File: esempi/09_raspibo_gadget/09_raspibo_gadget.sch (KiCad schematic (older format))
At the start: 20 parts, among them IC1 ATTINY85-S, P1 USB_OTG, P2 CONN_01X01, P3 CONN_01X01, P4 CONN_01X01, P5 CONN_01X01, P6 CONN_01X01, P7 CONN_01X01, P8 CONN_01X01, P9 CONN_01X01

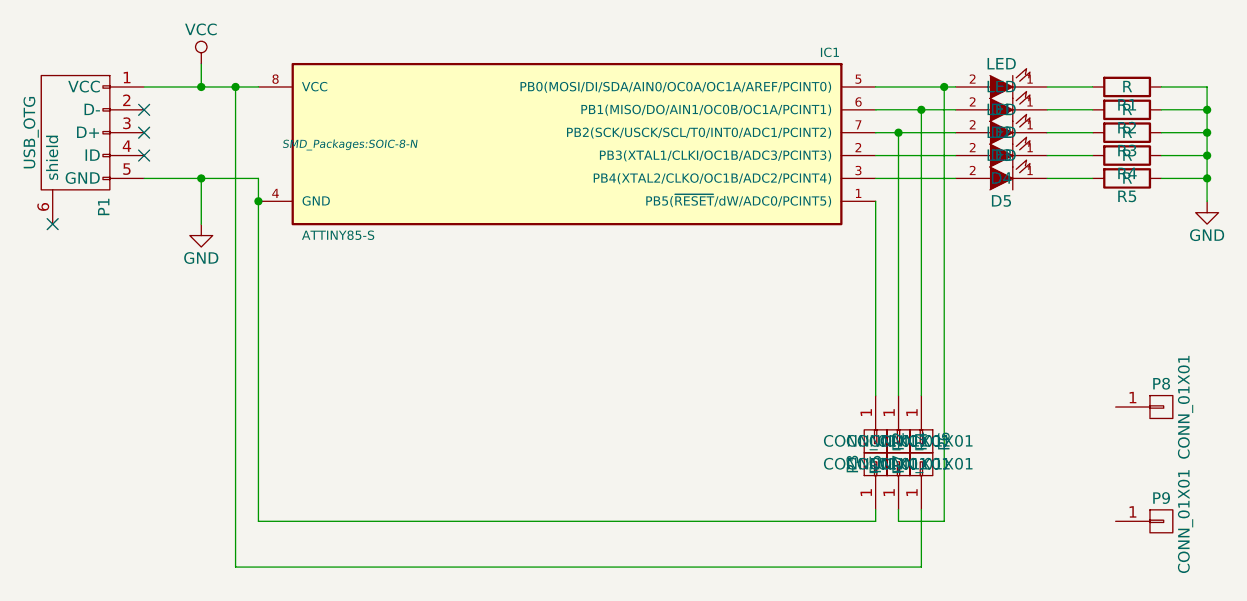
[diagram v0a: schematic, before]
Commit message: Modifiche a Raspibo gadget e L293D
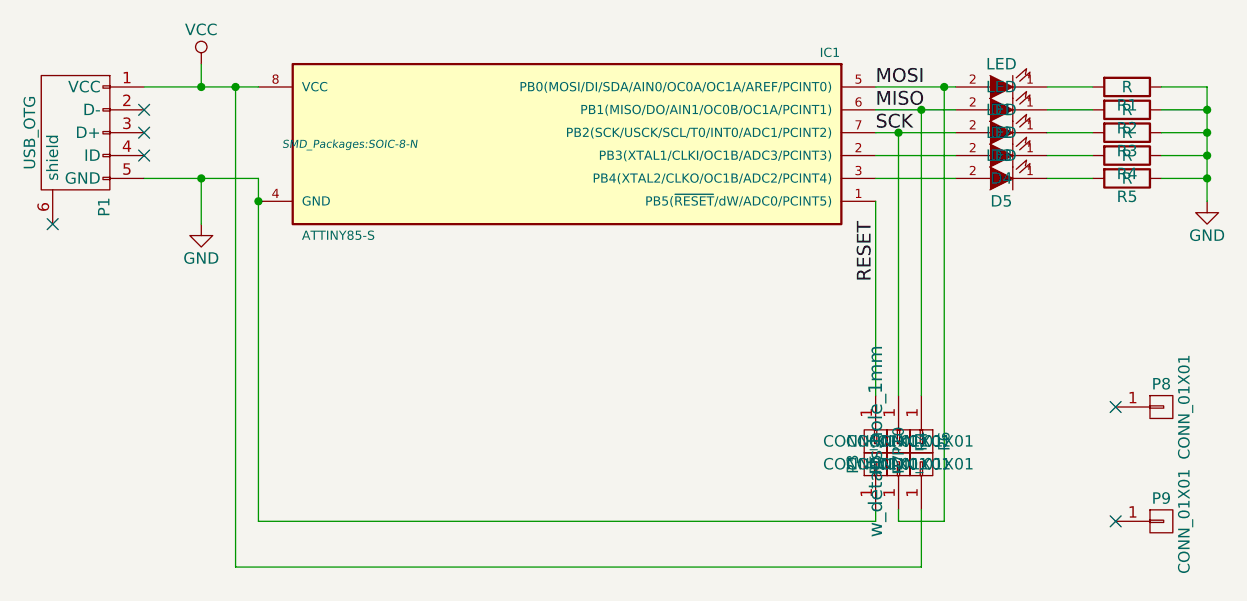
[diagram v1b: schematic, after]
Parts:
- removed P2: CONN_01X01, w_details:hole_1mm, symbol CONN_01X01
- added P10: CONN_01X01, w_details:hole_1mm, symbol CONN_01X01
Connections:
- net RESET: now reaches IC1.1 (PB5(~RESET~/dW/ADC0/PCINT5))
- net RESET: now also P10.1 (P1)
- net MOSI: now reaches D1.2 (A), IC1.5 (PB0(MOSI/DI/SDA/AIN0/OC0A/OC1A/AREF/PCINT0)), P5.1 (P1)
- net MISO: now reaches D2.2 (A), IC1.6 (PB1(MISO/DO/AIN1/OC0B/OC1A/PCINT1)), P6.1 (P1)
- net SCK: now reaches D3.2 (A), IC1.7 (PB2(SCK/USCK/SCL/T0/INT0/ADC1/PCINT2)), P4.1 (P1)
- no-connect marks 4 -> 6
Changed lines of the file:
@@
-$EndComp
-$Comp
-L CONN_01X01 P2
-U 1 1 5597C18B
-P 6600 4100
-F 0 "P2" H 6600 4200 50  0000 C CNN
-F 1 "CONN_01X01" V 6700 4100 50  0000 C CNN
-F 2 "w_details:hole_1mm" H 6600 4100 60  0001 C CNN
-F 3 "" H 6600 4100 60  0000 C CNN
-	1    6600 4100
-	0    1    1    0
 $EndComp
 $Comp
@@
 	0    -1   1    0
 $EndComp
+Text Label 6600 2550 0    60   ~ 0
+MOSI
+Text Label 6600 2650 0    60   ~ 0
+MISO
+Text Label 6600 2750 0    60   ~ 0
+SCK
+Text Label 6600 3400 1    60   ~ 0
+RESET
+NoConn ~ 7650 3950
+NoConn ~ 7650 4450
+$Comp
+L CONN_01X01 P10
+U 1 1 55C532DC
+P 6600 4100
+F 0 "P10" H 6600 4200 50  0000 C CNN
+F 1 "CONN_01X01" V 6700 4100 50  0000 C CNN
+F 2 "w_details:hole_1mm" H 6600 4100 60  0000 C CNN
+F 3 "" H 6600 4100 60  0000 C CNN
+	1    6600 4100
+	0    1    1    0
+$EndComp
 $EndSCHEMATC
